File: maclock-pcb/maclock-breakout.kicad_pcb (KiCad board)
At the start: 2 copper layers, 70.5 x 26.5 mm, 26 parts, among them J1 53398-0271, J2 53398-0471, J3 53398-0271, J4 Pi GPIO, SW1 TSB001A3518A, SW2 TSB001A3518A, U1 PAM8302AASCR, U2 SN74LVC1G17DBVR, U3 TPS7A2030PDBVR

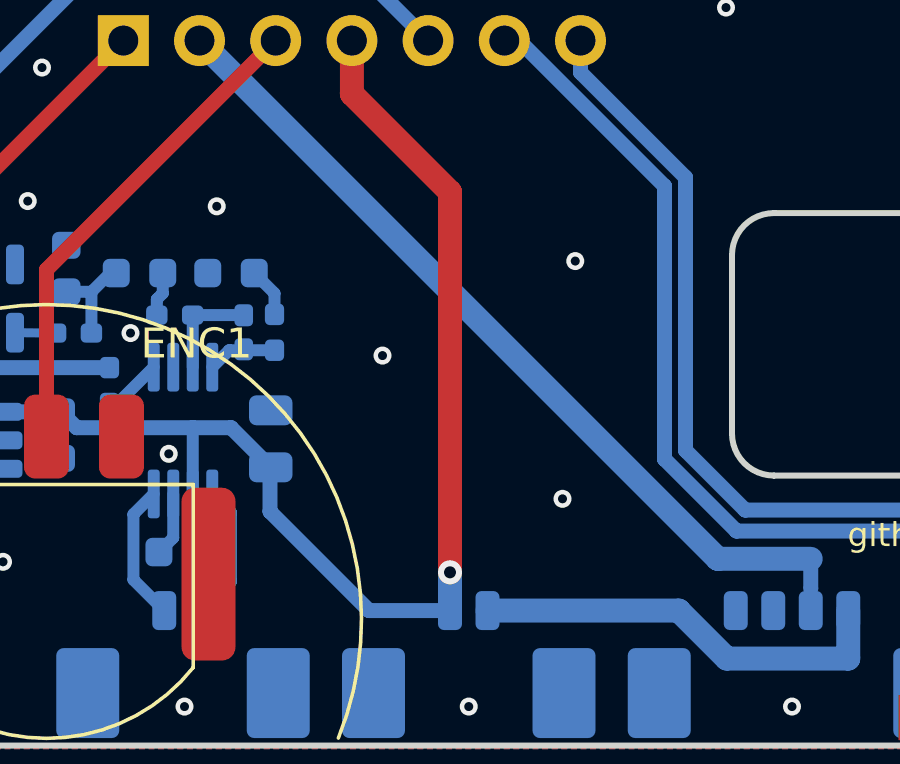
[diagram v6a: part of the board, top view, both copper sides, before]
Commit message: Breakout: second via on the +5V layer change at J1
The Pi's whole supply (about 1 A, 1.3 A peaks) goes from J1 pad 2 on
B.Cu to the F.Cu trunk here. A second 0.8/0.4 via at (140.35, 97.5),
1.225 mm north of the first and on the same trace, shares that current
so neither 0.4 mm hole carries it alone. DRC at baseline, 0 unconnected,
parity clean.
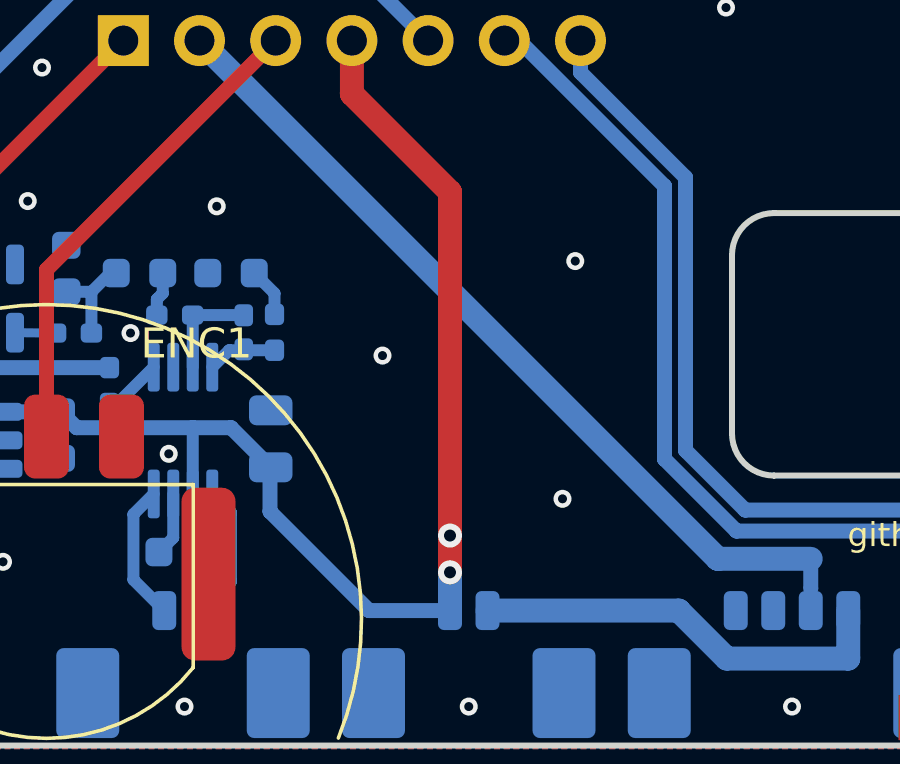
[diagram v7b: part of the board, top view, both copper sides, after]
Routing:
- net +5V: track 46.7 -> 47.9 mm, vias 1 -> 2
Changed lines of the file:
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@@
 	)
 	(segment
-		(start 140.35 98.725)
+		(start 140.35 97.5)
 		(end 140.35 86.047793)
 		(width 0.8)
@@
 		(width 0.8)
 		(layer "F.Cu")
+		(net "+5V")
+	)
+	(segment
+		(start 140.35 98.725)
+		(end 140.35 97.5)
+		(width 0.8)
+		(layer "F.Cu")
+		(net "+5V")
+	)
+	(via
+		(at 140.35 97.5)
+		(size 0.8)
+		(drill 0.4)
+		(layers "F.Cu" "B.Cu")
 		(net "+5V")
 	)
@@
 		(layer "B.Cu")
 		(net "+5V")
+	)
+	(segment
+		(start 140.35 98.725)
+		(end 140.35 97.5)
+		(width 0.8)
+		(layer "B.Cu")
+		(net "+5V")
